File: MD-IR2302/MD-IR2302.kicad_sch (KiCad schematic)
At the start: 19 parts, among them J1 XT60_Female_Horizontal, J2 Conn_01x03_Pin_signal, Q1 TK7R4A10PL_TabUp, Q2 TK7R4A10PL_TabUp, Q3 TK7R4A10PL_TabUp, Q4 TK7R4A10PL_TabUp, U1 IR2302, U2 IR2302

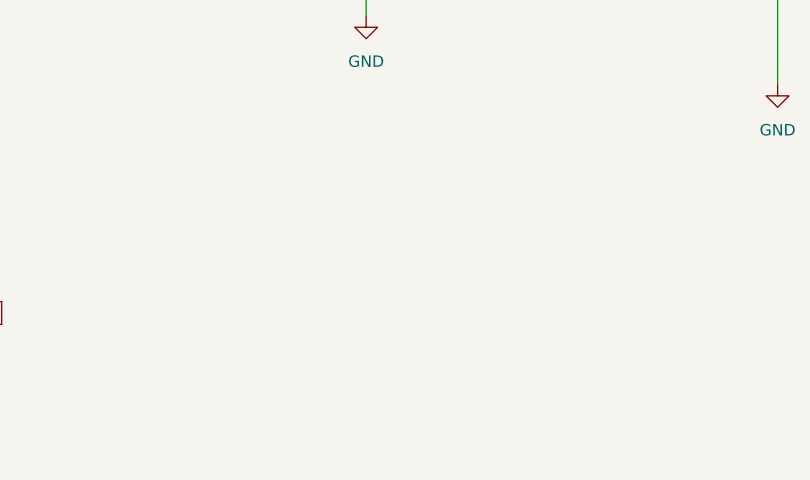
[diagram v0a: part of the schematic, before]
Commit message: ファン用電源を追加
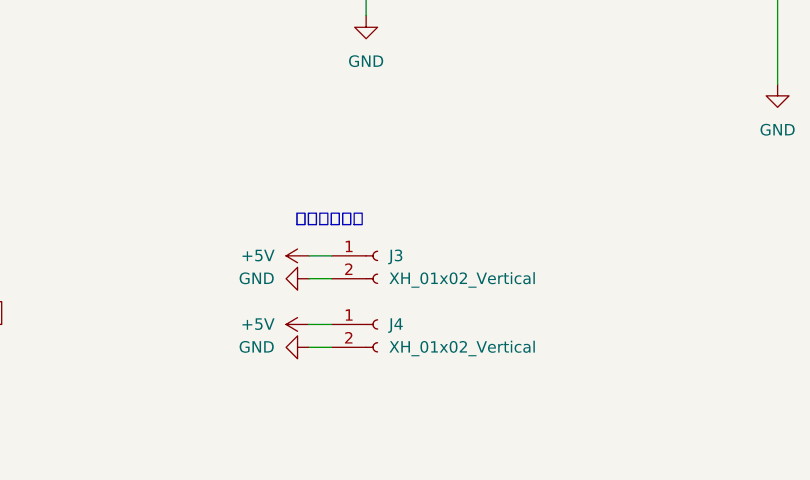
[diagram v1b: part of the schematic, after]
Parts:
- added J3, J4: XH_01x02_Vertical, Connector_JST:JST_XH_B2B-XH-A_1x02_P2.50mm_Vertical, symbol 00_mylib:XH_01x02
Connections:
- net +5V: now also J3.1 (Pin_1), J4.1 (Pin_1)
- net GND: now also J3.2 (Pin_2), J4.2 (Pin_2)
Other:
- note added: "ファン用電源"

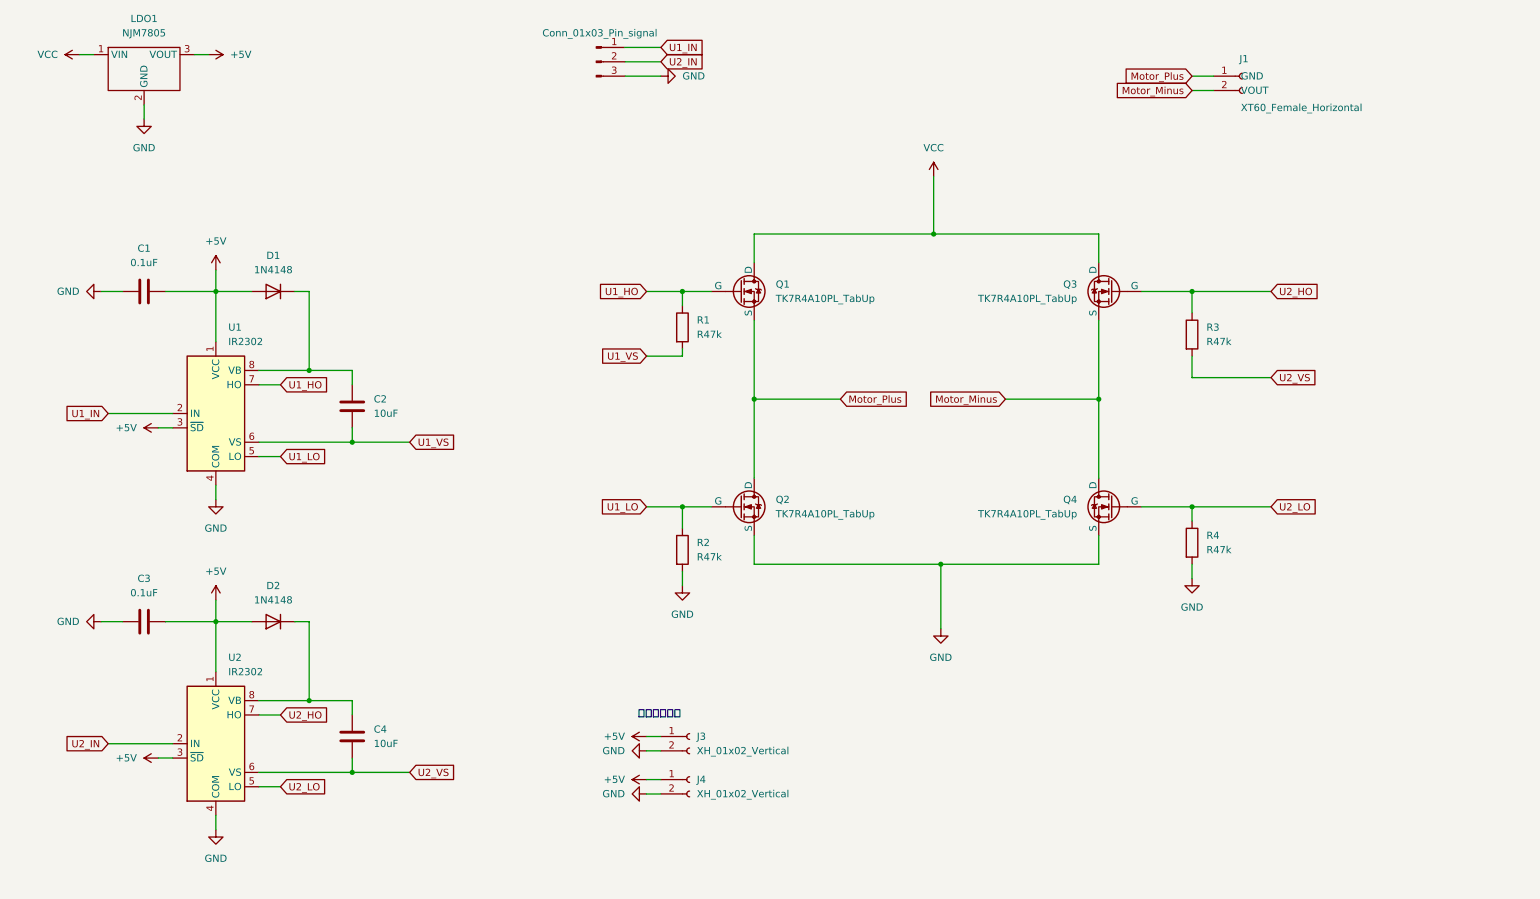
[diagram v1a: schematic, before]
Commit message: コンデンサを追加した
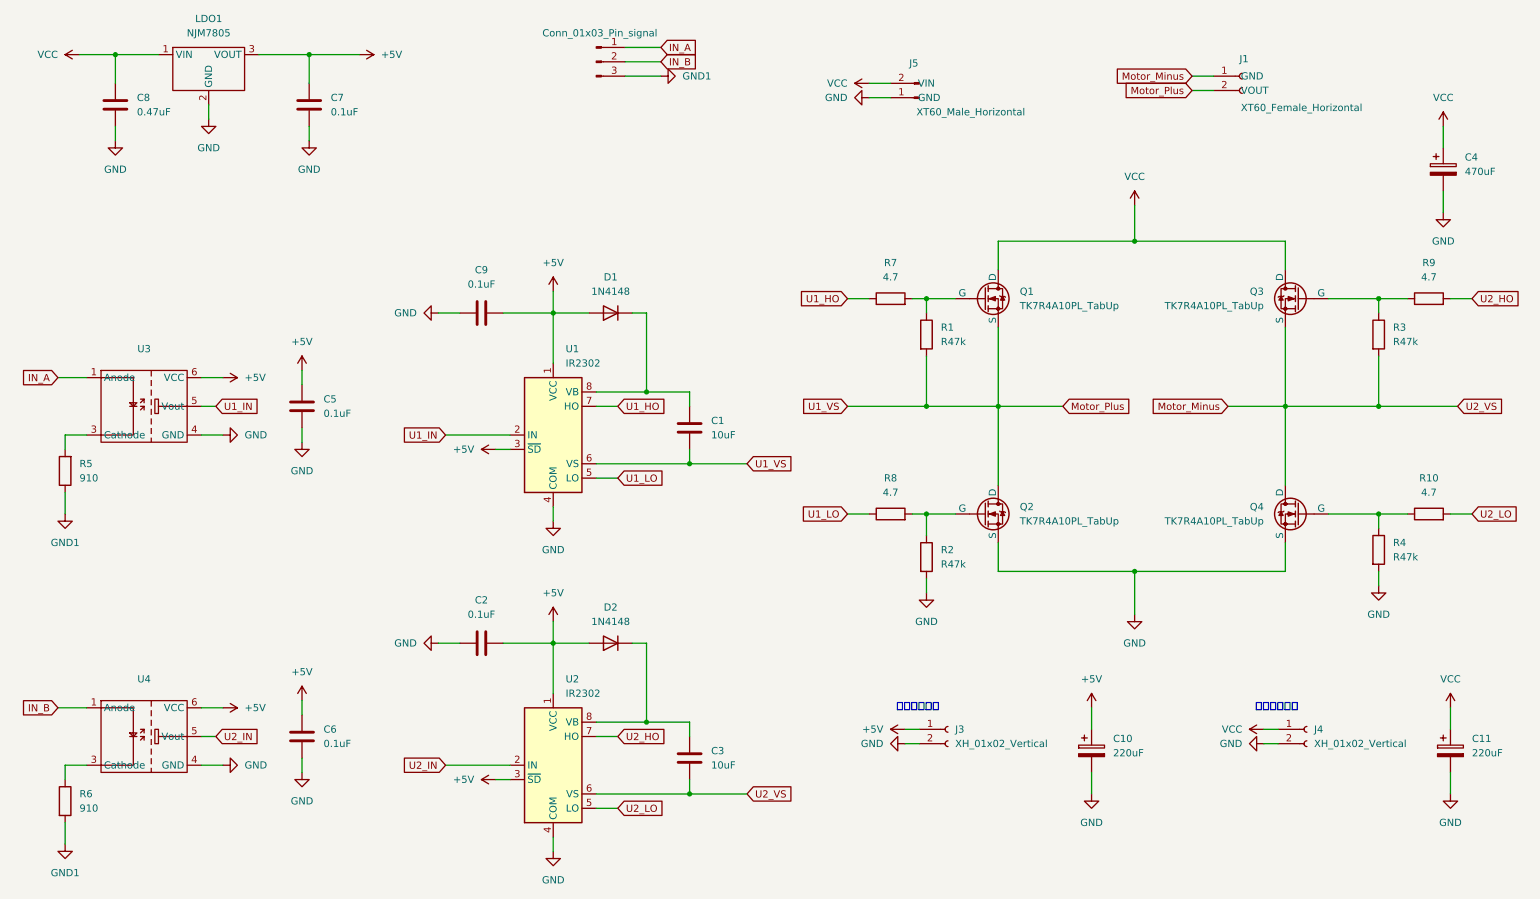
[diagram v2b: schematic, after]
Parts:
- removed C1, C3: 0.1uF, Capacitor_SMD:C_0603_1608Metric_Pad1.08x0.95mm_HandSolder, symbol 00_mylib:C1608
- removed C2, C4: 10uF, Capacitor_SMD:C_0603_1608Metric_Pad1.08x0.95mm_HandSolder, symbol 00_mylib:C1608
- added C1, C3: 10uF, Capacitor_SMD:C_0805_2012Metric_Pad1.18x1.45mm_HandSolder, symbol 00_mylib:C2012
- added C10, C11: 220uF, Capacitor_THT:CP_Radial_D8.0mm_P3.50mm, symbol 00_mylib:C_Polarized
- added C2, C5, C6, C7, C9: 0.1uF, Capacitor_SMD:C_0805_2012Metric_Pad1.18x1.45mm_HandSolder, symbol 00_mylib:C2012
- added C4: 470uF, Capacitor_THT:CP_Radial_D10.0mm_P5.00mm, symbol 00_mylib:C_Polarized
- added C8: 0.47uF, Capacitor_SMD:C_0805_2012Metric_Pad1.18x1.45mm_HandSolder, symbol 00_mylib:C2012
- added J5: XT60_Male_Horizontal, Connector_AMASS:AMASS_XT60PW-M_1x02_P7.20mm_Horizontal, symbol 00_mylib:XT60_Male_Horizontal
- added R10, R7, R8, R9: 4.7, Resistor_SMD:R_0603_1608Metric_Pad0.98x0.95mm_HandSolder, symbol 00_mylib:R1608
- added R5, R6: 910, Resistor_SMD:R_0603_1608Metric_Pad0.98x0.95mm_HandSolder, symbol 00_mylib:R1608
- added U3, U4: ~, Package_SO:MFSOP6-5_4.4x3.6mm_P1.27mm, symbol 00_mylib:TLP2361
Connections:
- net U1_VS is gone; now on net Motor_Plus: R1.2, U1.6 (VS)
- net U2_VS is gone; now on net Motor_Minus: R3.2, U2.6 (VS)
- net +5V: now also C10.1, C2.2, C5.2, C6.2, C7.2, C9.2, U3.6 (VCC), U4.6 (VCC); no longer J4.1 (Pin_1)
- net GND: now also C10.2, C11.2, C2.1, C4.2, C5.1, C6.1, C7.1, C8.2, C9.1, J5.1 (GND), U3.4 (GND), U4.4 (GND); no longer J2.3 (Pin_3)
- net Motor_Minus: now also J1.1 (GND), C3.2; no longer J1.2 (VOUT)
- net Motor_Plus: now also J1.2 (VOUT), C1.2; no longer J1.1 (GND)
- net U1_HO: now also R7.1; no longer Q1.2 (G), R1.1
- net U1_IN: now also U3.5 (Vout); no longer J2.1 (Pin_1)
- net U1_LO: now also R8.1; no longer Q2.2 (G), R2.1
- net U2_HO: now also R9.2; no longer Q3.2 (G), R3.1
- net U2_IN: now also U4.5 (Vout); no longer J2.2 (Pin_2)
- net U2_LO: now also R10.2; no longer Q4.2 (G), R4.1
- net VCC: now also J4.1 (Pin_1), C11.1, C4.1, C8.1, J5.2 (VIN)
- net at D2.1 (K), U2.8 (VB): now also C3.1
- net at D1.1 (K), U1.8 (VB): now also C1.1
- new net: Q3.2 (G), R3.1, R9.1
- new net: Q2.2 (G), R2.1, R8.2
- new net: R5.2, U3.3 (Cathode)
- new net: Q4.2 (G), R10.1, R4.1
- new net: R6.1, U4.3 (Cathode)
- new net: Q1.2 (G), R1.1, R7.2
- new net GND1: J2.3 (Pin_3), R5.1, R6.2
- new net IN_A: J2.1 (Pin_1), U3.1 (Anode)
- new net IN_B: J2.2 (Pin_2), U4.1 (Anode)
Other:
- company: (none) -> 明治大学オートメーション研究部
- title: (none) -> IR2302使用モータードライバ
- moved on the sheet: D1, D2, J3, LDO1, Q1, Q2, Q3, Q4, R1, R2, R3, R4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
